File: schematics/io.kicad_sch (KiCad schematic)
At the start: 13 parts, among them SW1 PEC12R, U1 NHD-C12832A1Z-FSRGB

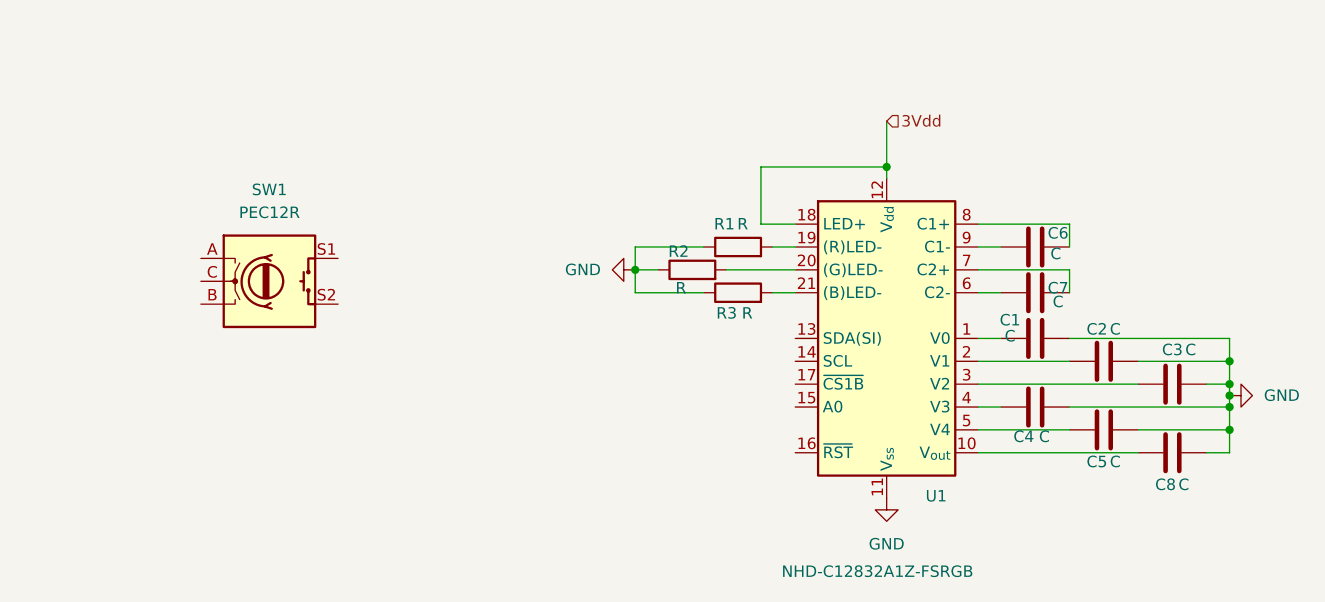
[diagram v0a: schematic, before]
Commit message: changed format to kicad project
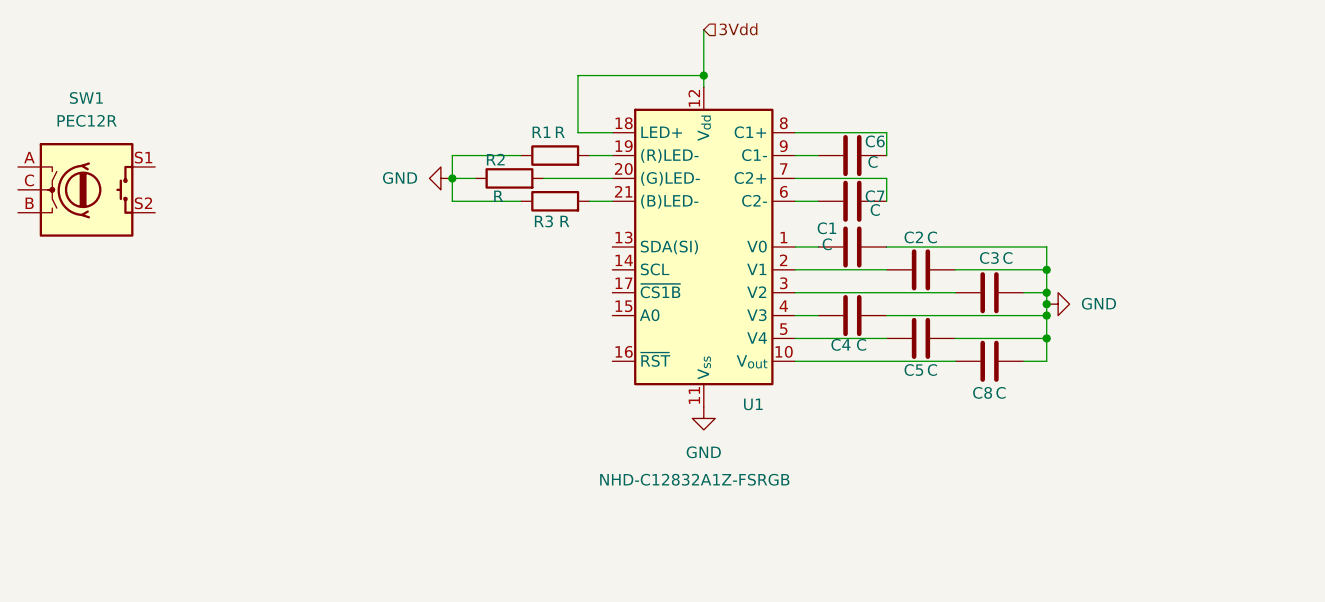
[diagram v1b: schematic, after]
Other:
- moved on the sheet: C1, C2, C3, C4, C5, C6, C7, C8, R1, R2, R3, SW1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
